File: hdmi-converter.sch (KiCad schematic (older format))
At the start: 127 parts, among them J2 46756-1001, Q1 BSS138APW, Q2 BSS138APW, Q3 BSS138APW, Q4 BSS138APW, U2 LT9611, U3 TXB0104RUT, U4 NTS0102GT, Y2 ABM8G-24.000MHZ-18-D2Y-T

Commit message: Loclib
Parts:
- R134, R137, R143, R58, R60, R61, R62, R87: symbol antmicroResistors0402:R_510R_0402 -> sa800u-baseboard-hw:R_510R_0402
- R140: symbol antmicroResistors0402:R_7k68_0402 -> sa800u-baseboard-hw:R_7k68_0402
- TP11, TP12, TP13, TP14, TP15, TP16, TP17, TP18, TP19, TP20, TP21, TP22, TP23, TP24, TP25, TP26, TP27, TP28, TP29, TP30: footprint antmicro-footprints:Testpoint_smd_0_75mm -> sa800u-baseboard-hw-footprints:Testpoint_smd_0_75mm; symbol antmicroTestPoints:TP_SMD_0_75MM -> sa800u-baseboard-hw:TP_SMD_0_75MM
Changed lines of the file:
@@
 	12425 7850 12425 7950
 $Comp
-L antmicroResistors0402:R_510R_0402 R58
+L sa800u-baseboard-hw:R_510R_0402 R58
 U 1 1 62395D6F
 P 12775 7700
@@
 $EndComp
 $Comp
-L antmicroResistors0402:R_510R_0402 R60
+L sa800u-baseboard-hw:R_510R_0402 R60
 U 1 1 623DE328
 P 13125 7700
@@
 $EndComp
 $Comp
-L antmicroResistors0402:R_510R_0402 R61
+L sa800u-baseboard-hw:R_510R_0402 R61
 U 1 1 623DE331
 P 13475 7700
@@
 $EndComp
 $Comp
-L antmicroResistors0402:R_510R_0402 R62
+L sa800u-baseboard-hw:R_510R_0402 R62
 U 1 1 62423F3E
 P 13825 7700
@@
 $EndComp
 $Comp
-L antmicroResistors0402:R_510R_0402 R87
+L sa800u-baseboard-hw:R_510R_0402 R87
 U 1 1 62423F47
 P 14175 7700
@@
 $EndComp
 $Comp
-L antmicroResistors0402:R_510R_0402 R134
+L sa800u-baseboard-hw:R_510R_0402 R134
 U 1 1 624698FA
 P 14525 7700
@@
 $EndComp
 $Comp
-L antmicroResistors0402:R_510R_0402 R137
+L sa800u-baseboard-hw:R_510R_0402 R137
 U 1 1 62469903
 P 14875 7700
@@
 LT9611_INTO_GPIO5
 $Comp
-L antmicroTestPoints:TP_SMD_0_75MM TP12
+L sa800u-baseboard-hw:TP_SMD_0_75MM TP12
 U 1 1 625051AE
 P 1400 1475
 F 0 "TP12" H 1400 1380 50  0000 C CNN
 F 1 "TP_SMD_0_75MM" H 1400 1375 50  0001 C CNN
-F 2 "antmicro-footprints:Testpoint_smd_0_75mm" H 1600 1675 60  0001 L CNN
+F 2 "sa800u-baseboard-hw-footprints:Testpoint_smd_0_75mm" H 1600 1675 60  0001 L CNN
 F 3 "" H 1600 1775 60  0001 L CNN
 	1    1400 1475
@@
 $EndComp
 $Comp
-L antmicroTestPoints:TP_SMD_0_75MM TP13
+L sa800u-baseboard-hw:TP_SMD_0_75MM TP13
 U 1 1 6254A343
 P 1400 2275
 F 0 "TP13" H 1400 2180 50  0000 C CNN
 F 1 "TP_SMD_0_75MM" H 1400 2175 50  0001 C CNN
-F 2 "antmicro-footprints:Testpoint_smd_0_75mm" H 1600 2475 60  0001 L CNN
+F 2 "sa800u-baseboard-hw-footprints:Testpoint_smd_0_75mm" H 1600 2475 60  0001 L CNN
 F 3 "" H 1600 2575 60  0001 L CNN
 	1    1400 2275
@@
 $EndComp
 $Comp
-L antmicroTestPoints:TP_SMD_0_75MM TP14
+L sa800u-baseboard-hw:TP_SMD_0_75MM TP14
 U 1 1 6258F43D
 P 1400 3050
 F 0 "TP14" H 1400 2955 50  0000 C CNN
 F 1 "TP_SMD_0_75MM" H 1400 2950 50  0001 C CNN
-F 2 "antmicro-footprints:Testpoint_smd_0_75mm" H 1600 3250 60  0001 L CNN
+F 2 "sa800u-baseboard-hw-footprints:Testpoint_smd_0_75mm" H 1600 3250 60  0001 L CNN
 F 3 "" H 1600 3350 60  0001 L CNN
 	1    1400 3050
@@
 $EndComp
 $Comp
-L antmicroTestPoints:TP_SMD_0_75MM TP19
+L sa800u-baseboard-hw:TP_SMD_0_75MM TP19
 U 1 1 625D4B94
 P 3900 1525
 F 0 "TP19" H 3900 1430 50  0000 C CNN
 F 1 "TP_SMD_0_75MM" H 3900 1425 50  0001 C CNN
-F 2 "antmicro-footprints:Testpoint_smd_0_75mm" H 4100 1725 60  0001 L CNN
+F 2 "sa800u-baseboard-hw-footprints:Testpoint_smd_0_75mm" H 4100 1725 60  0001 L CNN
 F 3 "" H 4100 1825 60  0001 L CNN
 	1    3900 1525
@@
 $EndComp
 $Comp
-L antmicroTestPoints:TP_SMD_0_75MM TP20
+L sa800u-baseboard-hw:TP_SMD_0_75MM TP20
 U 1 1 62619C3F
 P 3900 2325
 F 0 "TP20" H 3900 2230 50  0000 C CNN
 F 1 "TP_SMD_0_75MM" H 3900 2225 50  0001 C CNN
-F 2 "antmicro-footprints:Testpoint_smd_0_75mm" H 4100 2525 60  0001 L CNN
+F 2 "sa800u-baseboard-hw-footprints:Testpoint_smd_0_75mm" H 4100 2525 60  0001 L CNN
 F 3 "" H 4100 2625 60  0001 L CNN
 	1    3900 2325
@@
 $EndComp
 $Comp
-L antmicroTestPoints:TP_SMD_0_75MM TP21
+L sa800u-baseboard-hw:TP_SMD_0_75MM TP21
 U 1 1 6265ED54
 P 5775 2325
 F 0 "TP21" H 5775 2230 50  0000 C CNN
 F 1 "TP_SMD_0_75MM" H 5775 2225 50  0001 C CNN
-F 2 "antmicro-footprints:Testpoint_smd_0_75mm" H 5975 2525 60  0001 L CNN
+F 2 "sa800u-baseboard-hw-footprints:Testpoint_smd_0_75mm" H 5975 2525 60  0001 L CNN
 F 3 "" H 5975 2625 60  0001 L CNN
 	1    5775 2325
@@
 $EndComp
 $Comp
-L antmicroTestPoints:TP_SMD_0_75MM TP22
+L sa800u-baseboard-hw:TP_SMD_0_75MM TP22
 U 1 1 626AAEA8
 P 5825 4925
 F 0 "TP22" H 5825 4830 50  0000 C CNN
 F 1 "TP_SMD_0_75MM" H 5825 4825 50  0001 C CNN
-F 2 "antmicro-footprints:Testpoint_smd_0_75mm" H 6025 5125 60  0001 L CNN
+F 2 "sa800u-baseboard-hw-footprints:Testpoint_smd_0_75mm" H 6025 5125 60  0001 L CNN
 F 3 "" H 6025 5225 60  0001 L CNN
 	1    5825 4925
@@
 $EndComp
 $Comp
-L antmicroTestPoints:TP_SMD_0_75MM TP23
+L sa800u-baseboard-hw:TP_SMD_0_75MM TP23
 U 1 1 626EFB47
 P 6050 4925
 F 0 "TP23" H 6050 4830 50  0000 C CNN
 F 1 "TP_SMD_0_75MM" H 6050 4825 50  0001 C CNN
-F 2 "antmicro-footprints:Testpoint_smd_0_75mm" H 6250 5125 60  0001 L CNN
+F 2 "sa800u-baseboard-hw-footprints:Testpoint_smd_0_75mm" H 6250 5125 60  0001 L CNN
 F 3 "" H 6250 5225 60  0001 L CNN
 	1    6050 4925
@@
 	6050 5175 6600 5175
 $Comp
-L antmicroTestPoints:TP_SMD_0_75MM TP?
+L sa800u-baseboard-hw:TP_SMD_0_75MM TP?
 U 1 1 6280A6C8
 P 7275 6175
@@
 F 0 "TP25" V 7275 6125 50  0000 R CNN
 F 1 "TP_SMD_0_75MM" H 7275 6075 50  0001 C CNN
-F 2 "antmicro-footprints:Testpoint_smd_0_75mm" H 7475 6375 60  0001 L CNN
+F 2 "sa800u-baseboard-hw-footprints:Testpoint_smd_0_75mm" H 7475 6375 60  0001 L CNN
 F 3 "" H 7475 6475 60  0001 L CNN
 	1    7275 6175
@@
 $EndComp
 $Comp
-L antmicroTestPoints:TP_SMD_0_75MM TP?
+L sa800u-baseboard-hw:TP_SMD_0_75MM TP?
 U 1 1 628995FE
 P 7275 6075
@@
 F 0 "TP24" V 7275 6025 50  0000 R CNN
 F 1 "TP_SMD_0_75MM" H 7275 5975 50  0001 C CNN
-F 2 "antmicro-footprints:Testpoint_smd_0_75mm" H 7475 6275 60  0001 L CNN
+F 2 "sa800u-baseboard-hw-footprints:Testpoint_smd_0_75mm" H 7475 6275 60  0001 L CNN
 F 3 "" H 7475 6375 60  0001 L CNN
 	1    7275 6075
@@
 $EndComp
 $Comp
-L antmicroTestPoints:TP_SMD_0_75MM TP?
+L sa800u-baseboard-hw:TP_SMD_0_75MM TP?
 U 1 1 628E463D
 P 7275 8075
@@
 F 0 "TP26" V 7275 8025 50  0000 R CNN
 F 1 "TP_SMD_0_75MM" H 7275 7975 50  0001 C CNN
-F 2 "antmicro-footprints:Testpoint_smd_0_75mm" H 7475 8275 60  0001 L CNN
+F 2 "sa800u-baseboard-hw-footprints:Testpoint_smd_0_75mm" H 7475 8275 60  0001 L CNN
 F 3 "" H 7475 8375 60  0001 L CNN
 	1    7275 8075
@@
 $EndComp
 $Comp
-L antmicroTestPoints:TP_SMD_0_75MM TP?
+L sa800u-baseboard-hw:TP_SMD_0_75MM TP?
 U 1 1 6292E1E6
 P 1275 7875
@@
 F 0 "TP11" V 1275 7825 50  0000 R CNN
 F 1 "TP_SMD_0_75MM" H 1275 7775 50  0001 C CNN
-F 2 "antmicro-footprints:Testpoint_smd_0_75mm" H 1475 8075 60  0001 L CNN
+F 2 "sa800u-baseboard-hw-footprints:Testpoint_smd_0_75mm" H 1475 8075 60  0001 L CNN
 F 3 "" H 1475 8175 60  0001 L CNN
 	1    1275 7875
@@
 $EndComp
 $Comp
-L antmicroTestPoints:TP_SMD_0_75MM TP?
+L sa800u-baseboard-hw:TP_SMD_0_75MM TP?
 U 1 1 6297FFC8
 P 1425 5375
@@
 F 0 "TP15" H 1475 5422 50  0000 L CNN
 F 1 "TP_SMD_0_75MM" H 1425 5275 50  0001 C CNN
-F 2 "antmicro-footprints:Testpoint_smd_0_75mm" H 1625 5575 60  0001 L CNN
+F 2 "sa800u-baseboard-hw-footprints:Testpoint_smd_0_75mm" H 1625 5575 60  0001 L CNN
 F 3 "" H 1625 5675 60  0001 L CNN
 	1    1425 5375
@@
 $EndComp
 $Comp
-L antmicroTestPoints:TP_SMD_0_75MM TP?
+L sa800u-baseboard-hw:TP_SMD_0_75MM TP?
 U 1 1 62A0D2B6
 P 1725 5375
@@
 F 0 "TP16" H 1775 5422 50  0000 L CNN
 F 1 "TP_SMD_0_75MM" H 1725 5275 50  0001 C CNN
-F 2 "antmicro-footprints:Testpoint_smd_0_75mm" H 1925 5575 60  0001 L CNN
+F 2 "sa800u-baseboard-hw-footprints:Testpoint_smd_0_75mm" H 1925 5575 60  0001 L CNN
 F 3 "" H 1925 5675 60  0001 L CNN
 	1    1725 5375
@@
 $EndComp
 $Comp
-L antmicroTestPoints:TP_SMD_0_75MM TP?
+L sa800u-baseboard-hw:TP_SMD_0_75MM TP?
 U 1 1 62A99631
 P 2025 5375
@@
 F 0 "TP17" H 2075 5422 50  0000 L CNN
 F 1 "TP_SMD_0_75MM" H 2025 5275 50  0001 C CNN
-F 2 "antmicro-footprints:Testpoint_smd_0_75mm" H 2225 5575 60  0001 L CNN
+F 2 "sa800u-baseboard-hw-footprints:Testpoint_smd_0_75mm" H 2225 5575 60  0001 L CNN
 F 3 "" H 2225 5675 60  0001 L CNN
 	1    2025 5375
@@
 $EndComp
 $Comp
-L antmicroTestPoints:TP_SMD_0_75MM TP?
+L sa800u-baseboard-hw:TP_SMD_0_75MM TP?
 U 1 1 62AE01B3
 P 2350 5375
@@
 F 0 "TP18" H 2400 5422 50  0000 L CNN
 F 1 "TP_SMD_0_75MM" H 2350 5275 50  0001 C CNN
-F 2 "antmicro-footprints:Testpoint_smd_0_75mm" H 2550 5575 60  0001 L CNN
+F 2 "sa800u-baseboard-hw-footprints:Testpoint_smd_0_75mm" H 2550 5575 60  0001 L CNN
 F 3 "" H 2550 5675 60  0001 L CNN
 	1    2350 5375
@@
 	2350 5275 2350 4925
 $Comp
-L antmicroTestPoints:TP_SMD_0_75MM TP?
+L sa800u-baseboard-hw:TP_SMD_0_75MM TP?
 U 1 1 62CAF356
 P 9175 10025
@@
 F 0 "TP27" H 9126 10072 50  0000 R CNN
 F 1 "TP_SMD_0_75MM" H 9175 9925 50  0001 C CNN
-F 2 "antmicro-footprints:Testpoint_smd_0_75mm" H 9375 10225 60  0001 L CNN
+F 2 "sa800u-baseboard-hw-footprints:Testpoint_smd_0_75mm" H 9375 10225 60  0001 L CNN
 F 3 "" H 9375 10325 60  0001 L CNN
 	1    9175 10025
@@
 $EndComp
 $Comp
-L antmicroTestPoints:TP_SMD_0_75MM TP?
+L sa800u-baseboard-hw:TP_SMD_0_75MM TP?
 U 1 1 62CF6FE9
 P 9275 10025
@@
 F 0 "TP28" H 9325 10072 50  0000 L CNN
 F 1 "TP_SMD_0_75MM" H 9275 9925 50  0001 C CNN
-F 2 "antmicro-footprints:Testpoint_smd_0_75mm" H 9475 10225 60  0001 L CNN
+F 2 "sa800u-baseboard-hw-footprints:Testpoint_smd_0_75mm" H 9475 10225 60  0001 L CNN
 F 3 "" H 9475 10325 60  0001 L CNN
 	1    9275 10025
@@
 	9275 9925 9275 9725
 $Comp
-L antmicroTestPoints:TP_SMD_0_75MM TP?
+L sa800u-baseboard-hw:TP_SMD_0_75MM TP?
 U 1 1 62DCEB04
 P 11125 10025
@@
 F 0 "TP30" H 11076 10072 50  0000 R CNN
 F 1 "TP_SMD_0_75MM" H 11125 9925 50  0001 C CNN
-F 2 "antmicro-footprints:Testpoint_smd_0_75mm" H 11325 10225 60  0001 L CNN
+F 2 "sa800u-baseboard-hw-footprints:Testpoint_smd_0_75mm" H 11325 10225 60  0001 L CNN
 F 3 "" H 11325 10325 60  0001 L CNN
 	1    11125 10025
@@
 $EndComp
 $Comp
-L antmicroTestPoints:TP_SMD_0_75MM TP?
+L sa800u-baseboard-hw:TP_SMD_0_75MM TP?
 U 1 1 62DCEB0A
 P 11025 10025
@@
 F 0 "TP29" H 11075 10072 50  0000 L CNN
 F 1 "TP_SMD_0_75MM" H 11025 9925 50  0001 C CNN
-F 2 "antmicro-footprints:Testpoint_smd_0_75mm" H 11225 10225 60  0001 L CNN
+F 2 "sa800u-baseboard-hw-footprints:Testpoint_smd_0_75mm" H 11225 10225 60  0001 L CNN
 F 3 "" H 11225 10325 60  0001 L CNN
 	1    11025 10025
@@
 	11025 9925 11025 9725
 $Comp
-L antmicroResistors0402:R_7k68_0402 R140
+L sa800u-baseboard-hw:R_7k68_0402 R140
 U 1 1 629B0277
 P 3450 8275
@@
 $EndComp
 $Comp
-L antmicroResistors0402:R_510R_0402 R143
+L sa800u-baseboard-hw:R_510R_0402 R143
 U 1 1 622FF01E
 P 12425 7700

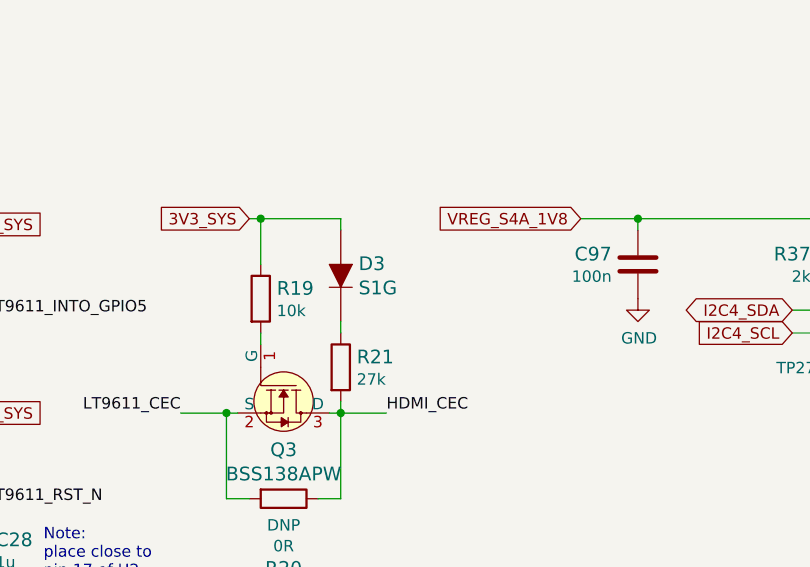
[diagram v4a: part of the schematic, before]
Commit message: Change D3 to N4148WS
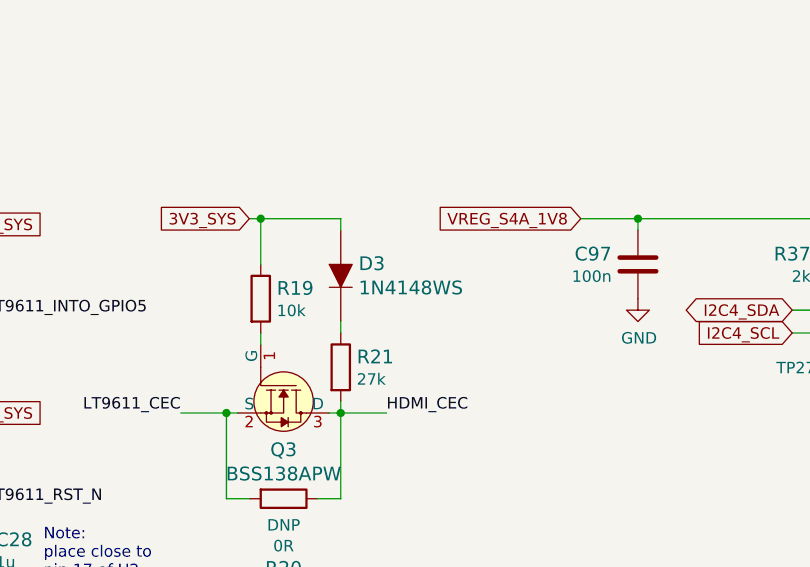
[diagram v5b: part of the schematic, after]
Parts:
- removed D3: S1G, sa800u-baseboard-hw-footprints:DO-214AC, symbol sa800u-baseboard-hw:S1G
- added D3: 1N4148WS, sa800u-baseboard-hw-footprints:SOD-323F, symbol sa800u-baseboard-hw:1N4148WS
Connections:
- net 3V3_SYS: now also D3.A
- net at R21.1: now also D3.K
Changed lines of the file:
@@
 Wire Wire Line
 	6700 9525 6700 9325
-$Comp
-L sa800u-baseboard-hw:S1G D3
-U 1 1 61AB5487
-P 7050 9575
-F 0 "D3" V 6997 9653 60  0000 L CNN
-F 1 "S1G" V 7103 9653 60  0000 L CNN
-F 2 "sa800u-baseboard-hw-footprints:DO-214AC" H 7250 9775 60  0001 L CNN
-F 3 "https://www.onsemi.com/pub/Collateral/S1M-D.pdf" H 7250 9875 60  0001 L CNN
-F 4 "S1G" H 7250 10075 60  0001 L CNN "MPN"
-F 5 "ON Semiconductor" H 7250 10675 60  0001 L CNN "Manufacturer"
-	1    7050 9575
-	0    1    1    0
-$EndComp
 Wire Wire Line
 	7050 9775 7050 9825
@@
 	0    1    1    0
 $EndComp
+$Comp
+L sa800u-baseboard-hw:1N4148WS D?
+U 1 1 62C88627
+P 7050 9575
+AR Path="/61A2F307/62C88627" Ref="D?"  Part="1"
+AR Path="/6197686D/62C88627" Ref="D3"  Part="1"
+F 0 "D3" V 6997 9497 60  0000 R CNN
+F 1 "1N4148WS" V 7103 9497 60  0000 R CNN
+F 2 "sa800u-baseboard-hw-footprints:SOD-323F" H 7250 9775 60  0001 L CNN
+F 3 "https://www.onsemi.com/pub/Collateral/1N914BWS-D.pdf" H 7250 9875 60  0001 L CNN
+F 4 "1N4148WS" H 7250 10075 60  0001 L CNN "MPN"
+F 5 "ON Semiconductor" H 7250 10675 60  0001 L CNN "Manufacturer"
+	1    7050 9575
+	0    -1   1    0
+$EndComp
 $EndSCHEMATC
